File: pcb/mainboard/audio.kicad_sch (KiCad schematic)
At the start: 40 parts, among them J701 Conn_01x02, J702 Conn_01x02, J703 AudioJack3_SwitchT, U701 WM8960

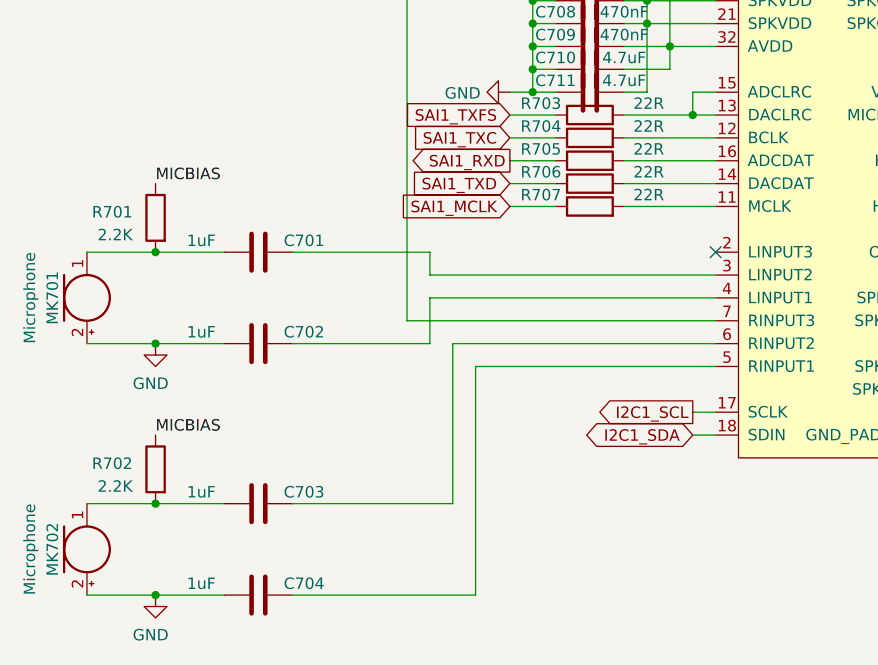
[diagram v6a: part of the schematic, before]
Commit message: - pcb: components placed
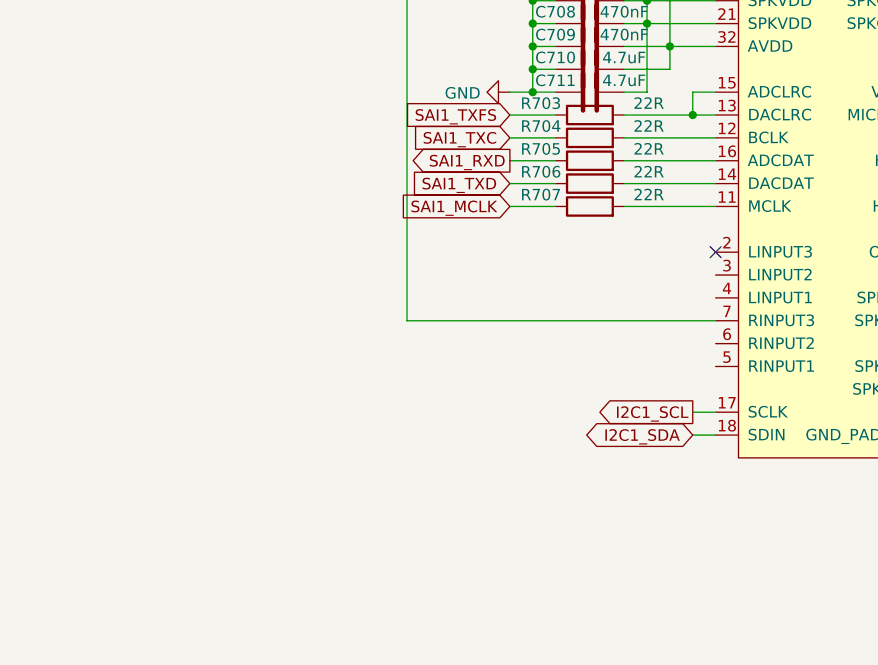
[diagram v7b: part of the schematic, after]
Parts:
- removed C701, C702, C703, C704: 1uF, Capacitor_SMD:C_0402_1005Metric, symbol Device:C
- removed MK701, MK702: Microphone, Connector_PinSocket_1.27mm:PinSocket_1x02_P1.27mm_Vertical, symbol Device:Microphone
- removed R701, R702: 2.2K, Resistor_SMD:R_0402_1005Metric, symbol Device:R
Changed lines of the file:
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@@
   (title_block
     (title "Archer Mainboard")
-    (date "2021-05-05")
+    (date "2021-05-06")
     (rev "R0.1 draft")
     (company "Copyright EI-2030 2021. / Engineer: Wenting Zhang")
@@
     (comment 4 "This source describes Open Hardware and is licensed under the CERN-OHL-S v2.")
   )
-  (junction (at 67.31 111.76) (diameter 0.9144) (color 0 0 0 0))
-  (junction (at 67.31 121.92) (diameter 0.9144) (color 0 0 0 0))
-  (junction (at 67.31 139.7) (diameter 0.9144) (color 0 0 0 0))
-  (junction (at 67.31 149.86) (diameter 0.9144) (color 0 0 0 0))
   (junction (at 109.22 81.28) (diameter 0.9144) (color 0 0 0 0))
   (junction (at 109.22 83.82) (diameter 0.9144) (color 0 0 0 0))
@@
   (no_connect (at 129.54 111.76))
   (no_connect (at 154.94 111.76))
-  (wire (pts (xy 59.69 111.76) (xy 67.31 111.76))
-    (stroke (width 0) (type solid) (color 0 0 0 0))
-  )
-  (wire (pts (xy 59.69 139.7) (xy 67.31 139.7))
-    (stroke (width 0) (type solid) (color 0 0 0 0))
-  )
-  (wire (pts (xy 67.31 121.92) (xy 59.69 121.92))
-    (stroke (width 0) (type solid) (color 0 0 0 0))
-  )
-  (wire (pts (xy 67.31 149.86) (xy 59.69 149.86))
-    (stroke (width 0) (type solid) (color 0 0 0 0))
-  )
-  (wire (pts (xy 74.93 111.76) (xy 67.31 111.76))
-    (stroke (width 0) (type solid) (color 0 0 0 0))
-  )
-  (wire (pts (xy 74.93 121.92) (xy 67.31 121.92))
-    (stroke (width 0) (type solid) (color 0 0 0 0))
-  )
-  (wire (pts (xy 74.93 139.7) (xy 67.31 139.7))
-    (stroke (width 0) (type solid) (color 0 0 0 0))
-  )
-  (wire (pts (xy 74.93 149.86) (xy 67.31 149.86))
-    (stroke (width 0) (type solid) (color 0 0 0 0))
-  )
-  (wire (pts (xy 82.55 149.86) (xy 102.87 149.86))
-    (stroke (width 0) (type solid) (color 0 0 0 0))
-  )
   (wire (pts (xy 95.25 73.66) (xy 95.25 119.38))
     (stroke (width 0) (type solid) (color 0 0 0 0))
@@
     (stroke (width 0) (type solid) (color 0 0 0 0))
   )
-  (wire (pts (xy 97.79 111.76) (xy 82.55 111.76))
-    (stroke (width 0) (type solid) (color 0 0 0 0))
-  )
-  (wire (pts (xy 97.79 114.3) (xy 97.79 111.76))
-    (stroke (width 0) (type solid) (color 0 0 0 0))
-  )
-  (wire (pts (xy 97.79 114.3) (xy 129.54 114.3))
-    (stroke (width 0) (type solid) (color 0 0 0 0))
-  )
-  (wire (pts (xy 97.79 116.84) (xy 97.79 121.92))
-    (stroke (width 0) (type solid) (color 0 0 0 0))
-  )
-  (wire (pts (xy 97.79 121.92) (xy 82.55 121.92))
-    (stroke (width 0) (type solid) (color 0 0 0 0))
-  )
-  (wire (pts (xy 100.33 121.92) (xy 100.33 139.7))
-    (stroke (width 0) (type solid) (color 0 0 0 0))
-  )
-  (wire (pts (xy 100.33 139.7) (xy 82.55 139.7))
-    (stroke (width 0) (type solid) (color 0 0 0 0))
-  )
-  (wire (pts (xy 102.87 124.46) (xy 129.54 124.46))
-    (stroke (width 0) (type solid) (color 0 0 0 0))
-  )
-  (wire (pts (xy 102.87 149.86) (xy 102.87 124.46))
-    (stroke (width 0) (type solid) (color 0 0 0 0))
-  )
   (wire (pts (xy 106.68 96.52) (xy 111.76 96.52))
     (stroke (width 0) (type solid) (color 0 0 0 0))
@@
     (stroke (width 0) (type solid) (color 0 0 0 0))
   )
-  (wire (pts (xy 129.54 116.84) (xy 97.79 116.84))
-    (stroke (width 0) (type solid) (color 0 0 0 0))
-  )
-  (wire (pts (xy 129.54 121.92) (xy 100.33 121.92))
-    (stroke (width 0) (type solid) (color 0 0 0 0))
-  )
   (wire (pts (xy 154.94 78.74) (xy 157.48 78.74))
     (stroke (width 0) (type solid) (color 0 0 0 0))
@@
   (wire (pts (xy 204.47 99.06) (xy 207.01 99.06))
     (stroke (width 0) (type solid) (color 0 0 0 0))
-  )
-  (label "MICBIAS" (at 67.31 104.14 0)
-    (effects (font (size 1.27 1.27)) (justify left bottom))
-  )
-  (label "MICBIAS" (at 67.31 132.08 0)
-    (effects (font (size 1.27 1.27)) (justify left bottom))
   )
   (label "MICBIAS" (at 166.37 96.52 180)
@@
     (pin "1")
   )
-  (symbol (lib_id "power:GND") (at 67.31 121.92 0) (mirror y) (unit 1)
-    (in_bom yes) (on_board yes)
-    (property "Reference" "#PWR0701" (id 0) (at 67.31 128.27 0)
-      (effects (font (size 1.27 1.27)) hide)
-    )
-    (property "Value" "GND" (id 1) (at 64.7701 126.365 0)
-      (effects (font (size 1.27 1.27)) (justify right))
-    )
-    (property "Footprint" "" (id 2) (at 67.31 121.92 0)
-      (effects (font (size 1.27 1.27)) hide)
-    )
-    (property "Datasheet" "" (id 3) (at 67.31 121.92 0)
-      (effects (font (size 1.27 1.27)) hide)
-    )
-    (pin "1")
-  )
-  (symbol (lib_id "power:GND") (at 67.31 149.86 0) (mirror y) (unit 1)
-    (in_bom yes) (on_board yes)
-    (property "Reference" "#PWR0702" (id 0) (at 67.31 156.21 0)
-      (effects (font (size 1.27 1.27)) hide)
-    )
-    (property "Value" "GND" (id 1) (at 64.7701 154.305 0)
-      (effects (font (size 1.27 1.27)) (justify right))
-    )
-    (property "Footprint" "" (id 2) (at 67.31 149.86 0)
-      (effects (font (size 1.27 1.27)) hide)
-    )
-    (property "Datasheet" "" (id 3) (at 67.31 149.86 0)
-      (effects (font (size 1.27 1.27)) hide)
-    )
-    (pin "1")
-  )
   (symbol (lib_id "power:GND") (at 106.68 93.98 270) (unit 1)
     (in_bom yes) (on_board yes)
@@
     (pin "2")
   )
-  (symbol (lib_id "Device:R") (at 67.31 107.95 0) (mirror y) (unit 1)
-    (in_bom yes) (on_board yes)
-    (property "Reference" "R701" (id 0) (at 64.77 107.3149 0)
-      (effects (font (size 1.27 1.27)) (justify left))
-    )
-    (property "Value" "2.2K" (id 1) (at 64.77 109.8549 0)
-      (effects (font (size 1.27 1.27)) (justify left))
-    )
-    (property "Footprint" "Resistor_SMD:R_0402_1005Metric" (id 2) (at 69.088 107.95 90)
-      (effects (font (size 1.27 1.27)) hide)
-    )
-    (property "Datasheet" "~" (id 3) (at 67.31 107.95 0)
-      (effects (font (size 1.27 1.27)) hide)
-    )
-    (pin "1")
-    (pin "2")
-  )
-  (symbol (lib_id "Device:R") (at 67.31 135.89 0) (mirror y) (unit 1)
-    (in_bom yes) (on_board yes)
-    (property "Reference" "R702" (id 0) (at 64.77 135.2549 0)
-      (effects (font (size 1.27 1.27)) (justify left))
-    )
-    (property "Value" "2.2K" (id 1) (at 64.77 137.7949 0)
-      (effects (font (size 1.27 1.27)) (justify left))
-    )
-    (property "Footprint" "Resistor_SMD:R_0402_1005Metric" (id 2) (at 69.088 135.89 90)
-      (effects (font (size 1.27 1.27)) hide)
-    )
-    (property "Datasheet" "~" (id 3) (at 67.31 135.89 0)
-      (effects (font (size 1.27 1.27)) hide)
-    )
-    (pin "1")
-    (pin "2")
-  )
   (symbol (lib_id "Device:R") (at 115.57 96.52 90) (unit 1)
     (in_bom yes) (on_board yes)
@@
     )
     (property "Datasheet" "~" (id 3) (at 210.82 124.46 0)
-      (effects (font (size 1.27 1.27)) hide)
-    )
-    (pin "1")
-    (pin "2")
-  )
-  (symbol (lib_id "Device:C") (at 78.74 111.76 270) (mirror x) (unit 1)
-    (in_bom yes) (on_board yes)
-    (property "Reference" "C701" (id 0) (at 83.82 110.49 90))
-    (property "Value" "1uF" (id 1) (at 72.39 110.49 90))
-    (property "Footprint" "Capacitor_SMD:C_0402_1005Metric" (id 2) (at 74.93 110.7948 0)
-      (effects (font (size 1.27 1.27)) hide)
-    )
-    (property "Datasheet" "~" (id 3) (at 78.74 111.76 0)
-      (effects (font (size 1.27 1.27)) hide)
-    )
-    (pin "1")
-    (pin "2")
-  )
-  (symbol (lib_id "Device:C") (at 78.74 121.92 270) (mirror x) (unit 1)
-    (in_bom yes) (on_board yes)
-    (property "Reference" "C702" (id 0) (at 83.82 120.65 90))
-    (property "Value" "1uF" (id 1) (at 72.39 120.65 90))
-    (property "Footprint" "Capacitor_SMD:C_0402_1005Metric" (id 2) (at 74.93 120.9548 0)
-      (effects (font (size 1.27 1.27)) hide)
-    )
-    (property "Datasheet" "~" (id 3) (at 78.74 121.92 0)
-      (effects (font (size 1.27 1.27)) hide)
-    )
-    (pin "1")
-    (pin "2")
-  )
-  (symbol (lib_id "Device:C") (at 78.74 139.7 270) (mirror x) (unit 1)
-    (in_bom yes) (on_board yes)
-    (property "Reference" "C703" (id 0) (at 83.82 138.43 90))
-    (property "Value" "1uF" (id 1) (at 72.39 138.43 90))
-    (property "Footprint" "Capacitor_SMD:C_0402_1005Metric" (id 2) (at 74.93 138.7348 0)
-      (effects (font (size 1.27 1.27)) hide)
-    )
-    (property "Datasheet" "~" (id 3) (at 78.74 139.7 0)
-      (effects (font (size 1.27 1.27)) hide)
-    )
-    (pin "1")
-    (pin "2")
-  )
-  (symbol (lib_id "Device:C") (at 78.74 149.86 270) (mirror x) (unit 1)
-    (in_bom yes) (on_board yes)
-    (property "Reference" "C704" (id 0) (at 83.82 148.59 90))
-    (property "Value" "1uF" (id 1) (at 72.39 148.59 90))
-    (property "Footprint" "Capacitor_SMD:C_0402_1005Metric" (id 2) (at 74.93 148.8948 0)
-      (effects (font (size 1.27 1.27)) hide)
-    )
-    (property "Datasheet" "~" (id 3) (at 78.74 149.86 0)
       (effects (font (size 1.27 1.27)) hide)
     )
@@
       (effects (font (size 1.27 1.27)) hide)
     )
-    (pin "1")
-    (pin "2")
-  )
-  (symbol (lib_id "Device:Microphone") (at 59.69 116.84 0) (mirror x) (unit 1)
-    (in_bom yes) (on_board yes)
-    (property "Reference" "MK701" (id 0) (at 55.88 116.84 90))
-    (property "Value" "Microphone" (id 1) (at 53.34 116.84 90))
-    (property "Footprint" "Connector_PinSocket_1.27mm:PinSocket_1x02_P1.27mm_Vertical" (id 2) (at 59.69 119.38 90)
-      (effects (font (size 1.27 1.27)) hide)
-    )
-    (property "Datasheet" "~" (id 3) (at 59.69 119.38 90)
-      (effects (font (size 1.27 1.27)) hide)
-    )
-    (pin "1")
-    (pin "2")
-  )
-  (symbol (lib_id "Device:Microphone") (at 59.69 144.78 0) (mirror x) (unit 1)
-    (in_bom yes) (on_board yes)
-    (property "Reference" "MK702" (id 0) (at 55.88 144.78 90))
-    (property "Value" "Microphone" (id 1) (at 53.34 144.78 90))
-    (property "Footprint" "Connector_PinSocket_1.27mm:PinSocket_1x02_P1.27mm_Vertical" (id 2) (at 59.69 147.32 90)
-      (effects (font (size 1.27 1.27)) hide)
-    )
-    (property "Datasheet" "~" (id 3) (at 59.69 147.32 90)
-      (effects (font (size 1.27 1.27)) hide)
-    )

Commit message: - pcb: finishing layout r0p1
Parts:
- U701: footprint Package_DFN_QFN:QFN-32-1EP_5x5mm_P0.5mm_EP3.6x3.6mm -> Package_DFN_QFN:QFN-32-1EP_5x5mm_P0.5mm_EP3.6x3.6mm_ThermalVias
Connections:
- net +1V8 is gone; now on net +3V3: C705.1, U701.8 (DCVDD)
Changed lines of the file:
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@@
   (junction (at 121.92 83.82) (diameter 0.9144) (color 0 0 0 0))
   (junction (at 121.92 86.36) (diameter 0.9144) (color 0 0 0 0))
+  (junction (at 124.46 63.5) (diameter 0.9144) (color 0 0 0 0))
   (junction (at 124.46 88.9) (diameter 0.9144) (color 0 0 0 0))
   (junction (at 127 78.74) (diameter 0.9144) (color 0 0 0 0))
@@
     (stroke (width 0) (type solid) (color 0 0 0 0))
   )
-  (wire (pts (xy 127 76.2) (xy 127 78.74))
+  (wire (pts (xy 127 63.5) (xy 124.46 63.5))
+    (stroke (width 0) (type solid) (color 0 0 0 0))
+  )
+  (wire (pts (xy 127 63.5) (xy 127 78.74))
     (stroke (width 0) (type solid) (color 0 0 0 0))
   )
@@
     (pin "1")
   )
-  (symbol (lib_id "power:+1V8") (at 127 76.2 0) (unit 1)
-    (in_bom yes) (on_board yes)
-    (property "Reference" "#PWR0706" (id 0) (at 127 80.01 0)
-      (effects (font (size 1.27 1.27)) hide)
-    )
-    (property "Value" "+1V8" (id 1) (at 127 72.39 0))
-    (property "Footprint" "" (id 2) (at 127 76.2 0)
-      (effects (font (size 1.27 1.27)) hide)
-    )
-    (property "Datasheet" "" (id 3) (at 127 76.2 0)
-      (effects (font (size 1.27 1.27)) hide)
-    )
-    (pin "1")
-  )
   (symbol (lib_id "power:+3.3VA") (at 204.47 66.04 0) (unit 1)
     (in_bom yes) (on_board yes)
@@
     (property "Reference" "U701" (id 0) (at 142.24 72.009 0))
     (property "Value" "WM8960" (id 1) (at 142.24 74.3204 0))
-    (property "Footprint" "Package_DFN_QFN:QFN-32-1EP_5x5mm_P0.5mm_EP3.6x3.6mm" (id 2) (at 142.24 73.66 0)
-      (effects (font (size 1.27 1.27)) hide)
-    )
+    (property "Footprint" "Package_DFN_QFN:QFN-32-1EP_5x5mm_P0.5mm_EP3.6x3.6mm_ThermalVias" (id 2) (at 142.24 73.66 0)
+      (effects (font (size 1.27 1.27)) hide)
+    )
